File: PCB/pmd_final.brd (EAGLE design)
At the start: 6.9 x 7.1 mm, 28 parts, among them IC1 MEGA128-A, IC4 REG1117, J1 DCJ0202, J2 RCA-LOCK, J3 RCA-LOCK, Q1 16 MHz

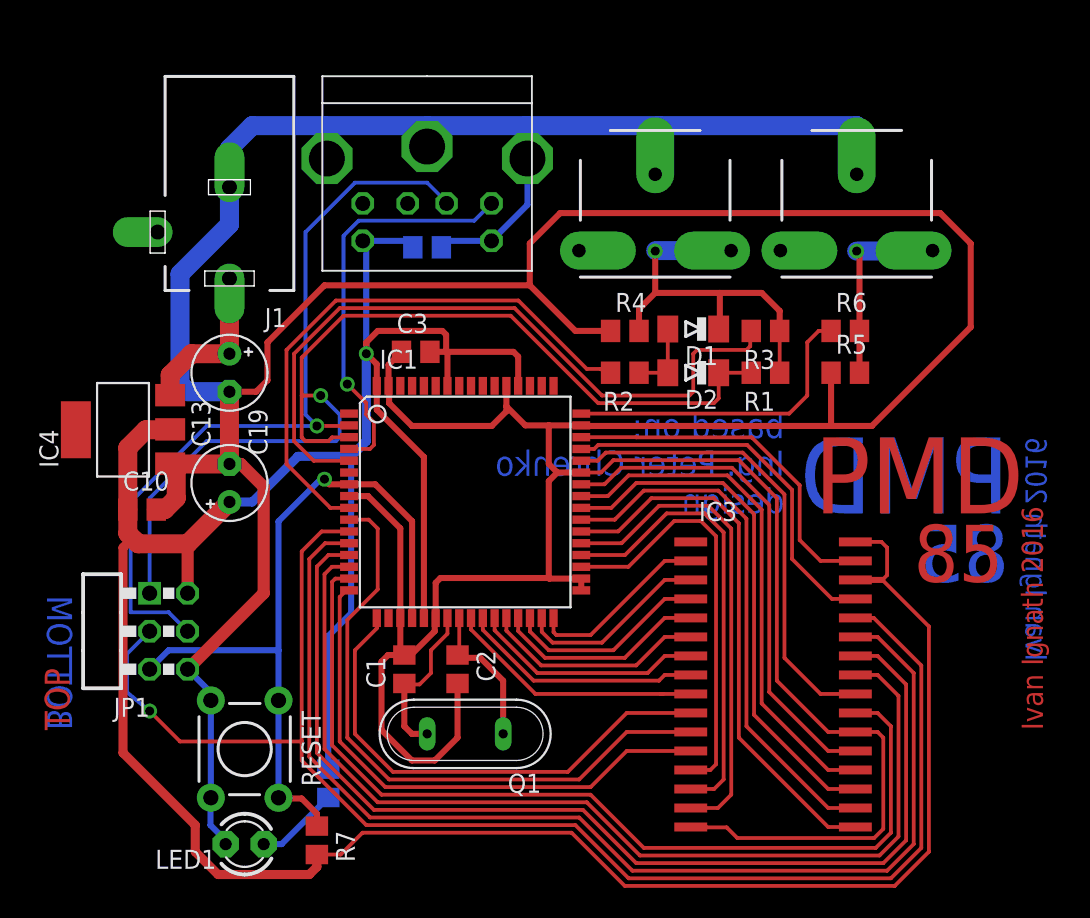
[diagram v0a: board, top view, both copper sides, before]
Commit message: fixed 2021 version
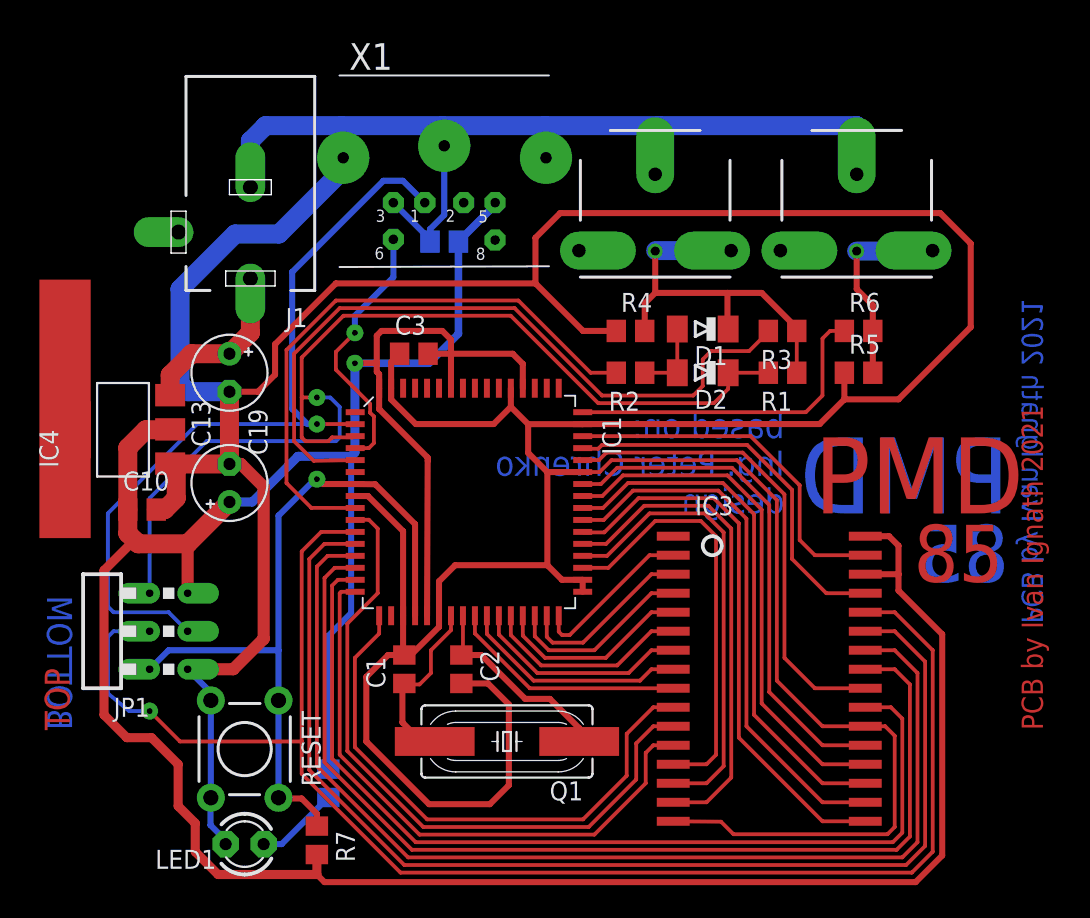
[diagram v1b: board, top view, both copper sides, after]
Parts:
- removed U$1: MINIDIN_6, connectors-digital:MINIDIN_6_3GND
- added X1: (no value), mini_din:M_DIN6
- IC1: value MEGA128-A -> MEGA128FIXED; device avr:TQFP64 -> avr:TQFP64_14X14MM
- IC3: device memory-sram:SOP32-N -> my_memory:SOP32L
- Q1: device special:QS -> crystal:HC49UP
- moved Q1 2.84 mm to (31.2, 9.91)
- moved J1 1.40 mm to (14.1, 43.9)
- moved C4 1.20 mm to (27.1, 43.3), turned to 180 degrees
- moved R1 1.14 mm to (49.7, 34.5)
- moved R3 1.14 mm to (49.7, 37.3)
- moved R5 0.89 mm to (54.7, 34.5)
- moved R6 0.89 mm to (54.7, 37.3)
- moved D1 0.63 mm to (44.3, 37.5)
- moved D2 0.63 mm to (44.3, 34.5)
- moved IC3 0.46 mm to (48.8, 14.1)
- moved R2 0.38 mm to (39.5, 34.5)
- moved R4 0.38 mm to (39.5, 37.3)
- moved IC1 0.25 mm to (28.7, 25.9), turned to 270 degrees
- moved C2 0.25 mm to (28.2, 14.7)
- moved C3 0.18 mm to (25.0, 35.8)
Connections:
- net GND: now also X1.3, X1.SH1, X1.SH2, X1.SH3; no longer U$1.3, U$1.CASE1, U$1.CASE2, U$1.SHIELDING
- net KB_CLK: now also X1.6; no longer U$1.5
- net KB_DATA(MOSI): now also X1.1; no longer U$1.1
- net VCC: now also X1.5; no longer U$1.4
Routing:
- net GND: track 366.2 -> 384.7 mm
- net KB_CLK: track 27.4 -> 17.6 mm
- net VCC: track 210.0 -> 218.4 mm
- net A15(SCK): track 98.8 -> 104.4 mm
- net A8: track 33.5 -> 37.5 mm
- net XTAL1: track 9.92 -> 13.5 mm
- net A10: track 36.5 -> 40.0 mm
- net A9: track 42.4 -> 45.5 mm
- net KB_DATA(MOSI): track 53.1 -> 55.8 mm
- net A14: track 76.9 -> 79.0 mm
- net A13: track 72.6 -> 74.7 mm
- net A12: track 68.2 -> 70.1 mm
- net A11: track 62.6 -> 64.3 mm
- net BRIGHT: track 38.1 -> 39.6 mm
- net A7: track 17.2 -> 15.9 mm
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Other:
- outline, holes or cut-outs redrawn
- board text added: "PCB by Ivan Ignath 2021"
- board text removed: "Ivan Ignath 2016"
